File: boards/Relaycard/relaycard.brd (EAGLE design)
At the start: 114.3 x 94 mm, 55 parts, among them IC1 ULN2801A, K1 NA, K2 NA, K3 NA, K4 NA, K5 NA, K6 NA, K7 NA, K8 NA, X1 112404, X10 112404, X11 112404, X12 112404, X13 112404, X14 112404, X15 112404, X16 112404, X2 112404, X3 112404, X4 112404, X5 112404, X6 112404, X7 112404, X8 112404, X9 112404

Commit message: Board update
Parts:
- moved K3 89.8 mm to (74.9, 2.54), turned to 180 degrees
- moved K2 88.9 mm to (92.7, 2.54), turned to 180 degrees
- moved X16 86.2 mm to (74.9, 17.8)
- moved X14 85.3 mm to (92.7, 17.8)
- moved OUTNEG 75.0 mm to (12.7, 68.6)
- moved OUTPOS 75.0 mm to (12.7, 53.3)
- moved X15 64.7 mm to (74.9, 35.6)
- moved X13 63.5 mm to (92.7, 35.6)
- moved D1 58.0 mm to (31.8, 72.4)
- moved JP1 46.8 mm to (96.5, 80.0)
- moved R1 46.6 mm to (36.8, 67.3)
- moved D4 45.8 mm to (17.8, 64.8)
- moved IC1 45.7 mm to (95.2, 69.8)
- moved R4 44.4 mm to (12.7, 69.8)
- moved D12 41.3 mm to (10.2, 72.4)
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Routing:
- net OUTPOS: track 253.6 -> 0.00 mm, vias 10 -> 0
- net OUTNEG: track 248.3 -> 14.8 mm, vias 9 -> 0
- net RELAY3: track 162.1 -> 0.00 mm, vias 1 -> 0
- net RELAY4: track 191.7 -> 39.3 mm, vias 1 -> 0
- net RELAY2: track 131.1 -> 0.00 mm, vias 1 -> 0
- net RELAY1: track 99.3 -> 0.00 mm, vias 1 -> 0
- net VCC: track 70.9 -> 169.2 mm, vias 9 -> 6
- net RELAY5: track 159.9 -> 119.1 mm, vias 3 -> 0
- net RELAY6: track 129.6 -> 99.2 mm, vias 3 -> 0
- net RELAY7: track 103.1 -> 80.0 mm, vias 3 -> 0
- net RELAY8: track 81.0 -> 58.6 mm, vias 3 -> 0
- net N$31: track 10.2 -> 30.6 mm
- net R4: track 10.2 -> 0.00 mm
- net N$35: track 10.2 -> 0.00 mm
- net N$33: track 10.2 -> 0.00 mm
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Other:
- board size 114.3 x 94 mm -> 127 x 106.7 mm

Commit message: Update experiments
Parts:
- moved D15 109.9 mm to (86.4, 2.54)
- moved R5 105.4 mm to (82.5, 0.00), turned to 0 degrees
- moved R6 101.2 mm to (100.3, 5.08)
- moved D8 100.6 mm to (82.5, 2.54), turned to 0 degrees
- moved D7 99.4 mm to (99.1, 1.27), turned to 0 degrees
- moved D16 98.0 mm to (100.3, 15.2)
- moved D1 77.3 mm to (64.8, 2.54), turned to 0 degrees
- moved R1 72.9 mm to (64.8, 0.00), turned to 0 degrees
- moved D12 70.0 mm to (15.2, 2.54)
- moved R4 69.9 mm to (11.4, 0.00), turned to 0 degrees
- moved D4 62.6 mm to (11.4, 2.54), turned to 0 degrees
- moved C1 56.1 mm to (77.5, 57.1)
- moved D14 34.3 mm to (74.9, 73.7), turned to 180 degrees
- moved R7 33.1 mm to (73.7, 71.1)
- moved D6 32.0 mm to (72.4, 67.3)
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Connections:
- removed net RELAY5: D12.A, IC1.14, K7.12, R4.1
- new net RELAY_8: D9.A, IC1.13, K4.12, R1.1
- net RELAY1: now also IC1.17; no longer IC1.18
- net RELAY2: now also IC1.18; no longer IC1.17
- net RELAY3: now also IC1.11; no longer IC1.16
- net RELAY4: now also IC1.12; no longer IC1.15
- net RELAY6: now also IC1.15; no longer IC1.13
- net RELAY7: now also IC1.14; no longer IC1.12
- net RELAY8: now also D12.A, IC1.16, K7.12, R4.1; no longer D9.A, IC1.11, K4.12, R1.1
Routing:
- net OUTNEG: track 14.8 -> 334.0 mm, vias 0 -> 8
- net VCC: track 169.2 -> 463.1 mm, vias 6 -> 9
- net OUTPOS: track 0.00 -> 229.7 mm, vias 0 -> 7
- net RELAY8: track 58.6 -> 222.4 mm, vias 0 -> 1
- net RELAY_8: track 0.00 -> 152.1 mm, vias 0 -> 1
- net RELAY5: track 119.1 -> 0.00 mm
- net RELAY6: track 99.2 -> 198.5 mm, vias 0 -> 1
- net RELAY7: track 80.0 -> 175.3 mm, vias 0 -> 1
- net RELAY4: track 39.3 -> 129.0 mm, vias 0 -> 1
- net RELAY3: track 0.00 -> 85.7 mm, vias 0 -> 1
- net RELAY2: track 0.00 -> 65.8 mm, vias 0 -> 1
- net RELAY1: track 0.00 -> 63.1 mm, vias 0 -> 1
- net N$31: track 30.6 -> 11.4 mm
- net N$44: track 0.00 -> 12.7 mm
- net N$42: track 0.00 -> 12.7 mm
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- added copper zone on layer 1, net GND
- removed copper zone on layer 1, net VCC
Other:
- board size 127 x 106.7 mm -> 127 x 100.3 mm
- board text added: "High"
- board text added: "Low"

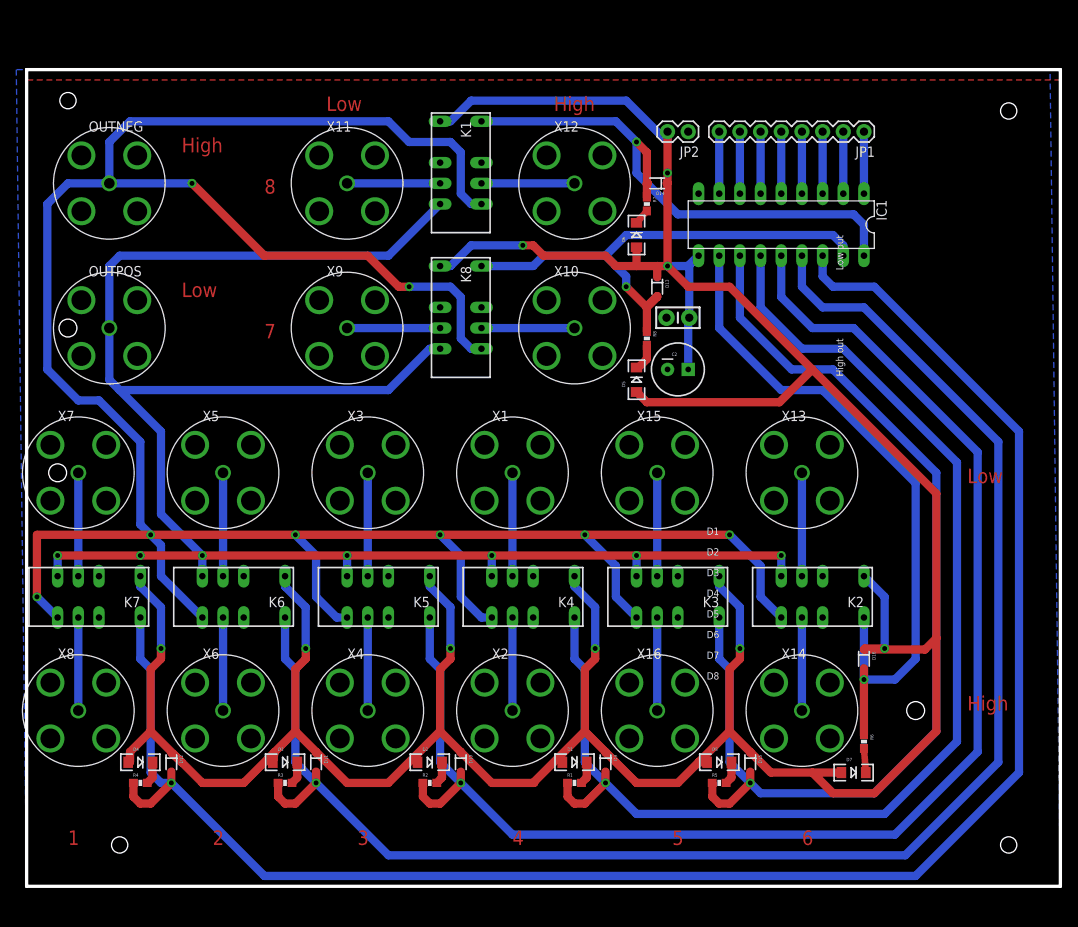
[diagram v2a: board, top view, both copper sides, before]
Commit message: Allow to remove methods
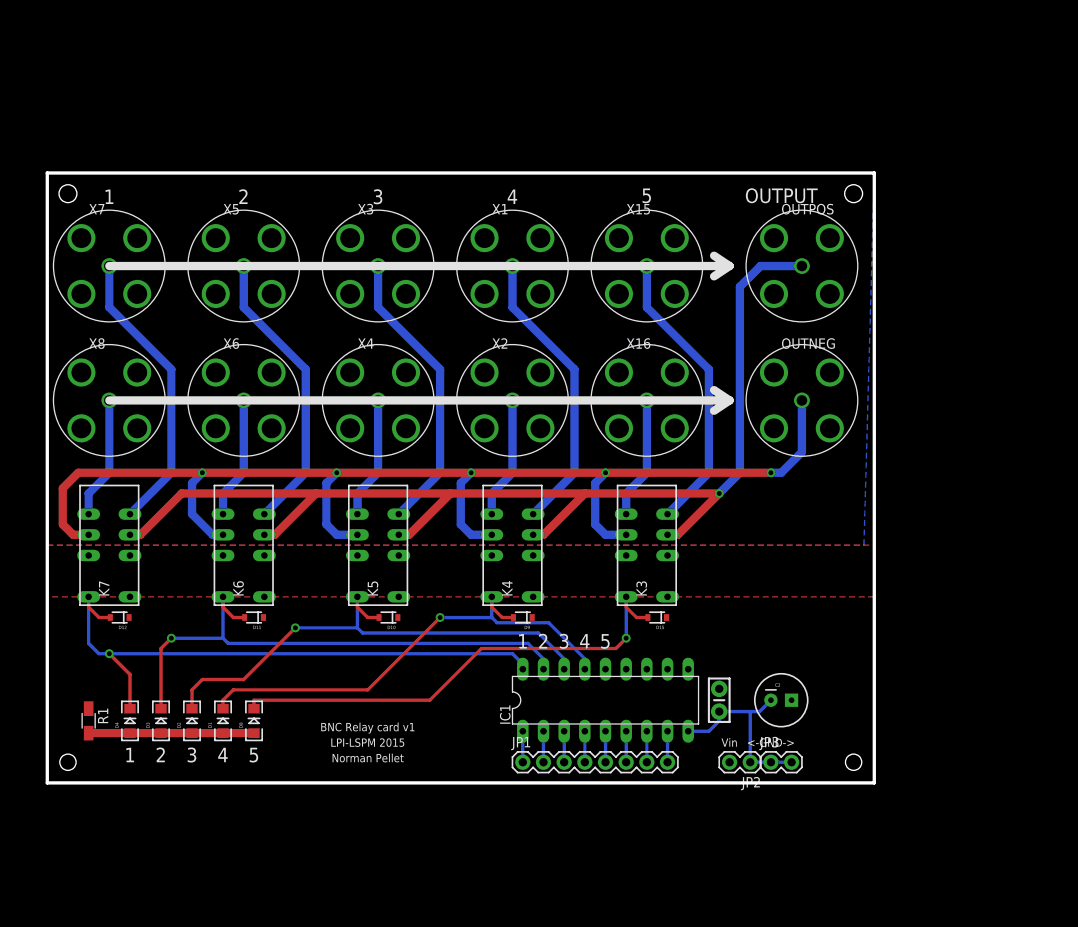
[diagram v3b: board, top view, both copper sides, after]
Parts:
- removed D13, D14, D16: 250mA/100V, SparkFun-DiscreteSemi:SOD-323
- removed D5, D6, D7: RED, SparkFun-LED:LED-1206
- removed K1, K2, K8: NA, relay:NA
- removed R2, R3, R4, R5, R6, R7, R8: 100/.25W, SparkFun-Resistors:0603-RES
- removed X10, X11, X12, X13, X14, X9: 112404, amphenol-112404_10:112404
- added JP3: (no value), SparkFun-Connectors:1X02
- R1: value 100/.25W -> (none); device SparkFun-Resistors:0603-RES -> resistor:R1206W
- moved OUTNEG 89.2 mm to (92.7, 47.0)
- moved JP1 88.1 mm to (58.4, 2.54), turned to 0 degrees
- moved OUTPOS 85.4 mm to (92.7, 63.5)
- moved JP2 77.8 mm to (86.4, 2.54)
- moved IC1 62.3 mm to (68.6, 10.2), turned to 0 degrees
- moved R1 60.2 mm to (5.08, 7.62), turned to 270 degrees
- moved D8 57.4 mm to (25.4, 7.62), turned to 90 degrees
- moved C1 47.3 mm to (82.5, 10.2), turned to 90 degrees
- moved D1 43.5 mm to (21.6, 7.62), turned to 90 degrees
- moved C2 42.6 mm to (90.2, 10.2)
- moved X8 38.3 mm to (7.62, 47.0)
- moved X6 38.2 mm to (24.1, 47.0)
- moved X16 38.1 mm to (73.7, 47.0)
- moved X4 38.1 mm to (40.6, 47.0)
- moved X2 38.1 mm to (57.1, 47.0)
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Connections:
- removed net N$13: D8.C, R5.2
- removed net N$16: D1.C, R1.2
- removed net N$17: D2.C, R2.2
- removed net N$19: D3.C, R3.2
- removed net N$22: D4.C, R4.2
- removed net N$31: K1.4, X11.1
- removed net N$32: K1.9, X12.1
- removed net N$33: K2.4, X13.1
- removed net N$34: K2.9, X14.1
- removed net N$35: K3.4, X15.1
- removed net N$36: K3.9, X16.1
- removed net N$37: K7.9, X8.1
- removed net N$38: K7.4, X7.1
- removed net N$39: K6.9, X6.1
- removed net N$40: K6.4, X5.1
- removed net N$41: K5.9, X4.1
- removed net N$42: K5.4, X3.1
- removed net N$43: K4.9, X2.1
- removed net N$44: K4.4, X1.1
- removed net R4: K8.4, X9.1
- removed net R5: K8.9, X10.1
- removed net RELAY_8: D9.A, IC1.13, K4.12, R1.1
- new net GND2: C1.1, C2.2, IC1.9, JP2.1, JP3.1, JP3.2
- new net N$1: K4.5, X1.1
- new net N$21: K7.5, X7.1
- new net N$23: K7.8, X8.1
- new net N$24: K3.5, X15.1
- new net N$25: K3.8, X16.1
- new net N$5: K5.8, X4.1
- new net N$7: K6.5, X5.1
- new net RELAY5: D15.A, D8.C, IC1.14, K3.12
- new net RES: D1.A, D2.A, D3.A, D4.A, D8.A, R1.2
- net GND: no longer C1.1, C2.2, IC1.9, JP2.1, X10.2, X10.3, X10.4, X10.5, X11.2, X11.3, X11.4, X11.5, X12.2, X12.3, X12.4, X12.5, X13.2, X13.3, X13.4, X13.5, X14.2, X14.3, X14.4, X14.5, X9.2, X9.3, X9.4, X9.5
- net N$14: now also K6.8, X6.1; no longer D5.C, R8.2
- net N$3: now also K4.8, X2.1; no longer D6.C, R7.2
- net N$4: now also K5.5, X3.1; no longer D7.C, R6.2
- net OUTNEG: now also K3.9, K4.9, K5.9, K6.9, K7.9; no longer K1.8, K2.8, K3.8, K4.8, K5.8, K6.8, K7.8, K8.8
- net OUTPOS: now also K3.4, K4.4, K5.4, K6.4, K7.4; no longer K1.5, K2.5, K3.5, K4.5, K5.5, K6.5, K7.5, K8.5
- net RELAY1: now also D12.A, D4.C, IC1.18, K7.12; no longer D13.A, IC1.17, K8.12, R8.1
- net RELAY2: now also D11.A, D3.C, IC1.17, K6.12; no longer D14.A, IC1.18, K1.12, R7.1
- net RELAY3: now also D10.A, D2.C, IC1.16, K5.12; no longer D16.A, IC1.11, K2.12, R6.1
- net RELAY4: now also D1.C, D9.A, IC1.15, K4.12; no longer D15.A, IC1.12, K3.12, R5.1
- net RELAY6: now also IC1.13; no longer D11.A, IC1.15, K6.12, R3.1
- net RELAY7: now also IC1.12; no longer D10.A, IC1.14, K5.12, R2.1
- net RELAY8: now also IC1.11; no longer D12.A, IC1.16, K7.12, R4.1
- net VCC: now also R1.1; no longer D1.A, D13.C, D14.C, D16.C, D2.A, D3.A, D4.A, D5.A, D6.A, D7.A, D8.A, K1.1, K2.1, K8.1
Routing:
- net VCC: track 463.1 -> 0.00 mm, vias 9 -> 0
- net RELAY8: track 222.4 -> 0.00 mm, vias 1 -> 0
- net RELAY6: track 198.5 -> 0.00 mm, vias 1 -> 0
- net OUTNEG: track 334.0 -> 151.2 mm, vias 8 -> 5
- net RELAY7: track 175.3 -> 0.00 mm, vias 1 -> 0
- net RELAY_8: track 152.1 -> 0.00 mm, vias 1 -> 0
- net OUTPOS: track 229.7 -> 143.4 mm, vias 7 -> 1
- net RELAY4: track 129.0 -> 60.1 mm
- net RELAY5: track 0.00 -> 59.5 mm, vias 0 -> 1
- net N$24: track 0.00 -> 35.7 mm
- net N$7: track 0.00 -> 35.7 mm
- net N$21: track 0.00 -> 35.7 mm
- net N$1: track 0.00 -> 35.7 mm
- net N$4: track 2.97 -> 35.7 mm
- net GND2: track 0.00 -> 23.7 mm
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- added copper zone on layer 1, net VCC
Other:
- board size 127 x 100.3 mm -> 101.6 x 74.9 mm
- board text added: "<-GND->"
- board text added: "BNC Relay card v1"
- board text added: "LPI-LSPM 2015"
- board text added: "Norman Pellet"
- board text added: "OUTPUT"
- board text added: "Vin"
- board text removed: "6"
- board text removed: "7"
- board text removed: "8"
- board text removed: "D1"
- board text removed: "D2"
- board text removed: "D3"
- board text removed: "D4"
- board text removed: "D5"
- board text removed: "D6"
- board text removed: "D7"
- board text removed: "D8"
- board text removed: "High"
- board text removed: "High out"
- board text removed: "Low"
- board text removed: "Low out"
